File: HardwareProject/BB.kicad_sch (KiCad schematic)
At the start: 61 parts, among them J10 Conn_01x01, J11 Conn_01x01, J12 Conn_01x01, J9 Conn_01x01, Q1 HYG080N10LS1C2, Q2 HYG080N10LS1C2, Q3 HYG080N10LS1C2, Q4 HYG080N10LS1C2, U1 UCC27211ADRMR, U18 UCC27519, U2 UCC27211ADRMR, U3 UCC27519

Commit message: 修改了UCC27211A封装，此芯片此前的封装均错误 修改了采样线布局，为SAR ADC加入前置RC
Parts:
- U1, U2: footprint HPM6P41_BB:VSON-8-1EP_3x3mm_P0.65mm_EP1.65x2.4mm -> TexasInstruments:DRM8_3P38X2P45_TEX
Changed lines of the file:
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@@
 			)
 		)
-		(property "Footprint" "HPM6P41_BB:VSON-8-1EP_3x3mm_P0.65mm_EP1.65x2.4mm"
+		(property "Footprint" "TexasInstruments:DRM8_3P38X2P45_TEX"
 			(at 46.99 119.38 0)
 			(effects
@@
 			)
 		)
-		(property "Footprint" "HPM6P41_BB:VSON-8-1EP_3x3mm_P0.65mm_EP1.65x2.4mm"
+		(property "Footprint" "TexasInstruments:DRM8_3P38X2P45_TEX"
 			(at 138.43 119.38 0)
 			(effects

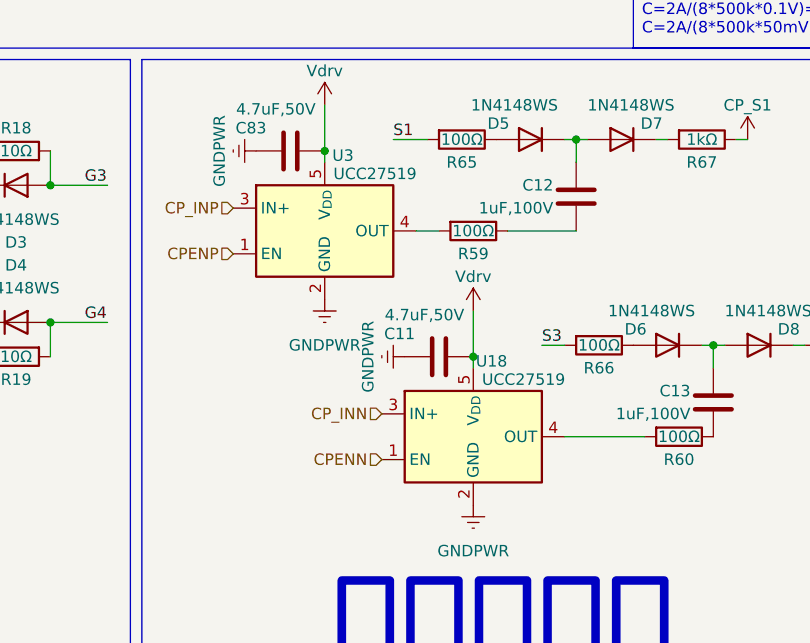
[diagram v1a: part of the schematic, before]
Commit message: 换掉UCC27519，它居然要55%VDD才到逻辑高，换成UCC2751
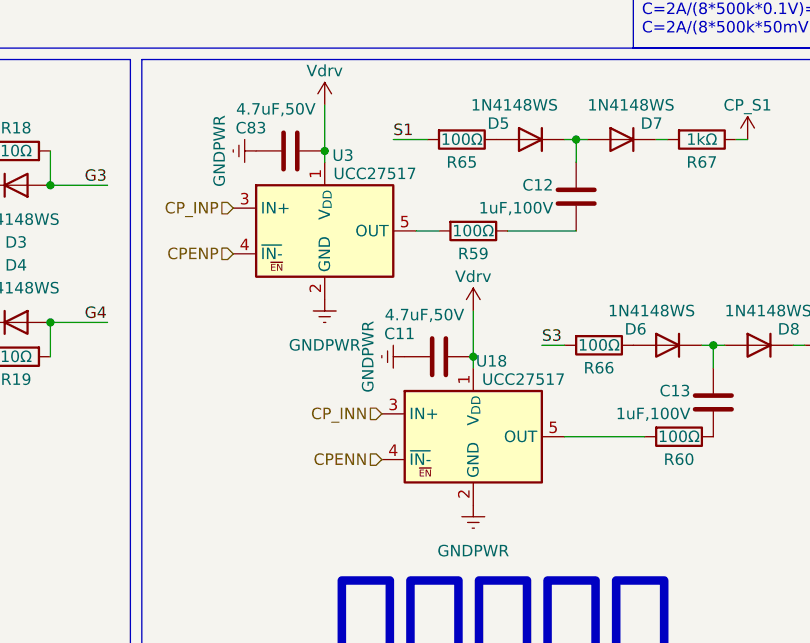
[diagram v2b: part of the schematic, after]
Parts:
- U18, U3: value UCC27519 -> UCC27517
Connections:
- net CPENN: now also U18.4 (~{IN-}); no longer U18.1 (EN)
- net CPENP: now also U3.4 (~{IN-}); no longer U3.1 (EN)
- net Vdrv: now also U18.1 (V_{DD}), U3.1 (V_{DD}); no longer U18.5 (V_{DD}), U3.5 (V_{DD})
- net at R60.2: now also U18.5 (OUT); no longer U18.4 (OUT)
- net at R59.2: now also U3.5 (OUT); no longer U3.4 (OUT)
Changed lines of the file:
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@@
+	)
+	(symbol
+		(lib_name "UCC27518_UCC27519_1")
+		(lib_id "1MyICs:UCC27518_UCC27519")
+		(at 236.22 140.97 0)
+		(unit 1)
+		(exclude_from_sim no)
+		(in_bom yes)
+		(on_board yes)
+		(dnp no)
+		(property "Reference" "U18"
+			(at 238.252 132.588 0)
+			(effects
+				(font
+					(size 1.27 1.27)
+				)
+			)
+		)
+		(property "Value" "UCC27517"
+			(at 241.808 134.62 0)
+			(effects
+				(font
+					(size 1.27 1.27)
+				)
+			)
+		)
+		(property "Footprint" "Package_TO_SOT_SMD:SOT-23-5"
+			(at 236.22 153.035 0)
+			(effects
+				(font
+					(size 1.27 1.27)
+				)
+				(hide yes)
+			)
+		)
+		(property "Datasheet" "https://www.ti.com.cn/cn/lit/ds/symlink/ucc27519.pdf?ts=1747047529320&ref_url=https%253A%252F%252Fwww.ti.com.cn%252Fproduct%252Fcn%252FUCC27519"
+			(at 236.22 121.92 0)
+			(effects
+				(font
+					(size 1.27 1.27)
+				)
+				(hide yes)
+			)
+		)
+		(property "Description" "Single-Channel High-Speed Low-Side Gate Driver With 4-A Peak Source and 8-A Peak Sink, SOT-23-6"
+			(at 236.22 140.97 0)
+			(effects
+				(font
+					(size 1.27 1.27)
+				)
+				(hide yes)
+			)
+		)
+		(pin "3"
+		)
+		(pin "1"
+		)
+		(pin "4"
+		)
+		(pin "5"
+		)
+		(pin "2"
+		)
+		(instances
+			(project "HPM6P41_BB"
+				(path "/714b8a30-f9a7-49d4-a000-bc20c4884c7a/89c5bb8e-77b8-47ed-968d-36636acd2e72"
+					(reference "U18")
+					(unit 1)
+				)
+			)
+		)
 	)
 	(symbol
@@
 	)
 	(symbol
-		(lib_id "1MyICs:UCC27518_UCC27519")
-		(at 236.22 140.97 0)
-		(unit 1)
-		(exclude_from_sim no)
-		(in_bom yes)
-		(on_board yes)
-		(dnp no)
-		(property "Reference" "U18"
-			(at 238.252 132.588 0)
-			(effects
-				(font
-					(size 1.27 1.27)
-				)
-			)
-		)
-		(property "Value" "UCC27519"
-			(at 241.808 134.62 0)
-			(effects
-				(font
-					(size 1.27 1.27)
-				)
-			)
-		)
-		(property "Footprint" "Package_TO_SOT_SMD:SOT-23-5"
-			(at 236.22 153.035 0)
-			(effects
-				(font
-					(size 1.27 1.27)
-				)
-				(hide yes)
-			)
-		)
-		(property "Datasheet" "https://www.ti.com.cn/cn/lit/ds/symlink/ucc27519.pdf?ts=1747047529320&ref_url=https%253A%252F%252Fwww.ti.com.cn%252Fproduct%252Fcn%252FUCC27519"
-			(at 236.22 121.92 0)
-			(effects
-				(font
-					(size 1.27 1.27)
-				)
-				(hide yes)
-			)
-		)
-		(property "Description" "Single-Channel High-Speed Low-Side Gate Driver With 4-A Peak Source and 8-A Peak Sink, SOT-23-6"
-			(at 236.22 140.97 0)
-			(effects
-				(font
-					(size 1.27 1.27)
-				)
-				(hide yes)
-			)
-		)
-		(pin "3"
-		)
-		(pin "1"
-		)
-		(pin "4"
-		)
-		(pin "5"
-		)
-		(pin "2"
-		)
-		(instances
-			(project "HPM6P41_BB"
-				(path "/714b8a30-f9a7-49d4-a000-bc20c4884c7a/89c5bb8e-77b8-47ed-968d-36636acd2e72"
-					(reference "U18")
-					(unit 1)
-				)
-			)
-		)
-	)
-	(symbol
 		(lib_id "power:+12V")
 		(at 27.94 113.03 0)
@@
 	)
 	(symbol
+		(lib_name "UCC27518_UCC27519_1")
 		(lib_id "1MyICs:UCC27518_UCC27519")
 		(at 219.71 118.11 0)
@@
 			)
 		)
-		(property "Value" "UCC27519"
+		(property "Value" "UCC27517"
 			(at 225.298 111.76 0)
 			(effects
@@
 		(instances
 			(project ""
-				(path "/714b8a30-f9a7-49d4-a000-bc20c4884c7a/89c5bb8e-77b8-47ed-968d-36636acd2e72"
+				(path "/714b8a30-f9a7-49d4-a000-bc20c4884c7a/5ba70b1a-2680-42f0-98ce-27de27e994eb"
 					(reference "U3")
+					(unit 1)
+				)
+				(path "/714b8a30-f9a7-49d4-a000-bc20c4884c7a/89c5bb8e-77b8-47ed-968d-36636acd2e72"
+					(reference "U3")

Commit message: Rev3最终版本
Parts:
- added TP1, TP2, TP3, TP4: TestPoint_Probe, HPM6P41_BB:TestPoint_Bridge_Pitch1.2mm_Drill0.7mm, symbol Connector:TestPoint_Probe
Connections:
- net IN1: now also TP3.1
- net IN2: now also TP4.1
- net IN3: now also TP1.1
- net IN4: now also TP2.1

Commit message: 换其他电感之前暂存一下
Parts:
- removed R17: 1mΩ 5W, HPM6P41_BB:R_Shunt_2725_2726, symbol Device:R_Shunt
- added C80, C84, C85, C94: 100V 100uF, Capacitor_THT:CP_Radial_D10.0mm_P5.00mm, symbol Device:C_Polarized
- C10, C3, C4, C9: footprint HPM6P41_BB:CP_Radial_D10.0mm_P5.00mm -> Capacitor_THT:CP_Radial_D10.0mm_P5.00mm
- L1: value CPU2916-6R8MC/VER2923-682KL -> PQ26XX; footprint HPM6P41_BB:IND_VER2923_COC -> HPM6P41_BB:PQ26XX
- TP1, TP2, TP3, TP4: footprint HPM6P41_BB:TestPoint_Bridge_Pitch1.2mm_Drill0.7mm -> HPM6P41_BB:测试点
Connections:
- net GNDPWR: now also C80.2, C84.2, C85.2, C94.2
- net S1: now also L1.2; no longer L1.1
- net S3: now also R10.1; no longer L1.2
- net VIN: now also Q1.5 (D), C85.1, C94.1; no longer R10.1
- net VOUT: now also Q3.5 (D), C80.1, C84.1
- net at R10.4: now also L1.1; no longer Q1.5 (D)
- net InputIsense+ renamed ISENSE-
- net InputIsense- renamed ISENSE+
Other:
- moved on the sheet: C8, C9, J11, J12, L1, Q3, Q4, R10, R15, R16, R20, R21

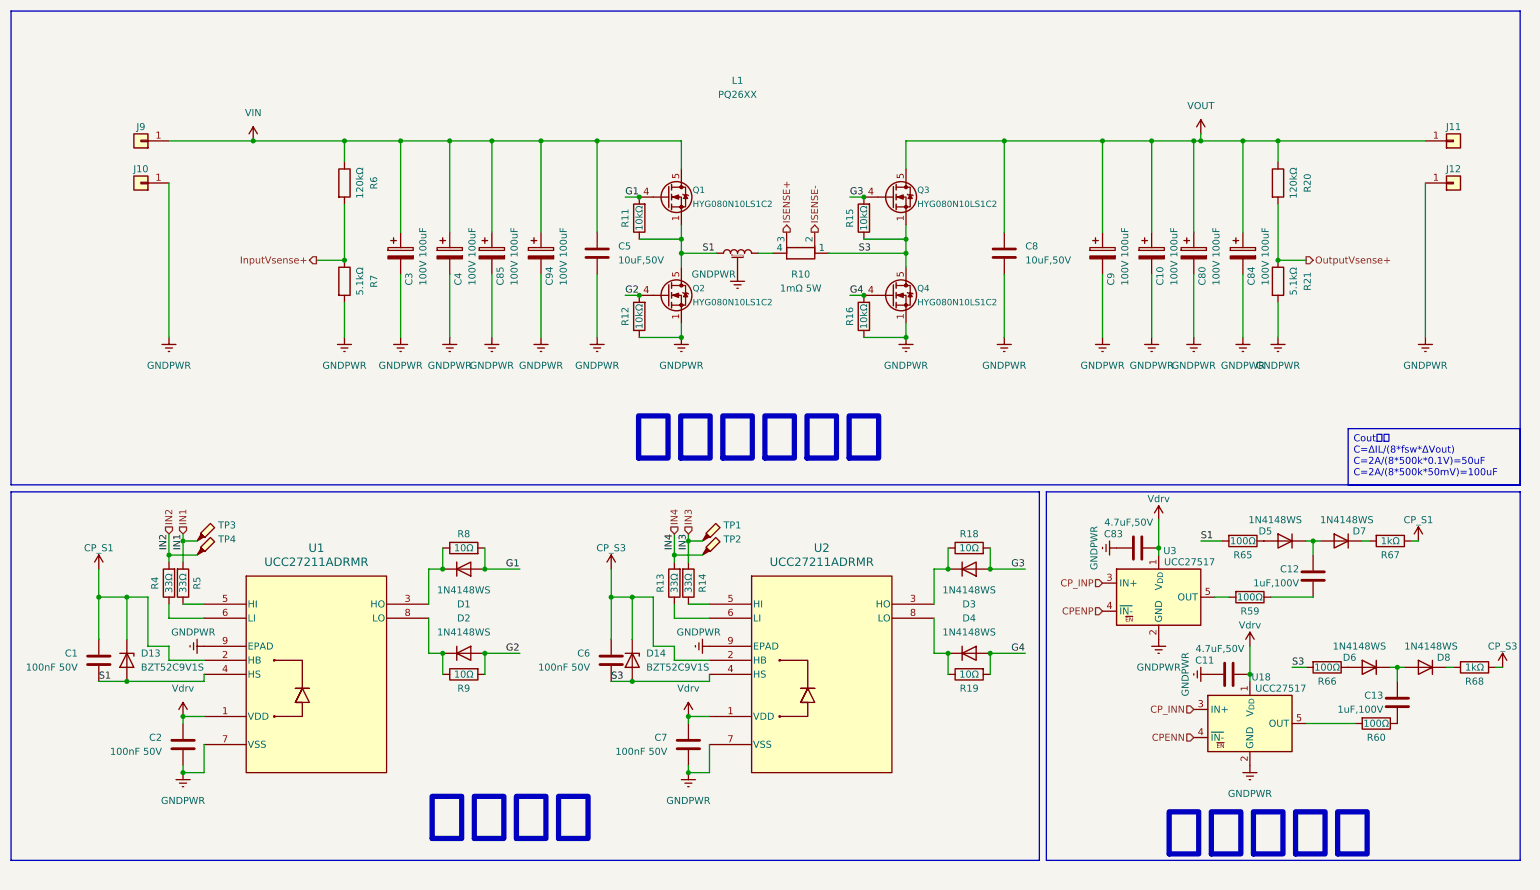
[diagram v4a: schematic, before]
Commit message: 完成Rev4 电源 驱动 模拟 IO
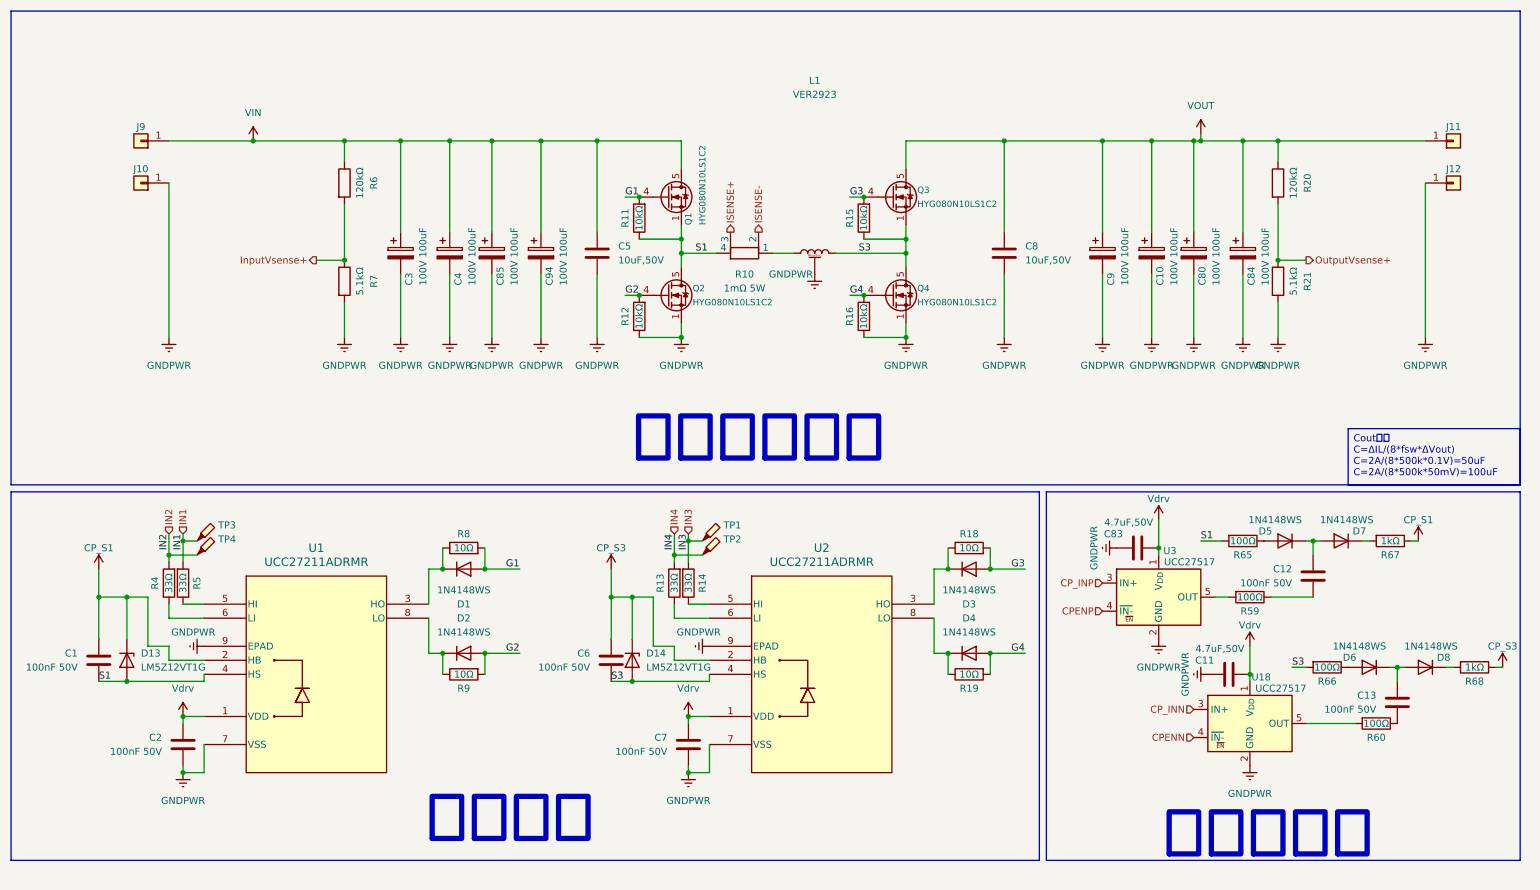
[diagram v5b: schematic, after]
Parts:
- C12, C13: value 1uF,100V -> 100nF 50V; footprint Capacitor_SMD:C_0805_2012Metric -> Capacitor_SMD:C_0603_1608Metric
- D1, D2, D3, D4, D5, D6, D7, D8: footprint Diode_SMD:D_SOD-323 -> Diode_SMD:D_SOD-523
- D13, D14: value BZT52C9V1S -> LM5Z12VT1G; footprint Diode_SMD:D_SOD-323 -> Diode_SMD:D_SOD-523
- L1: value PQ26XX -> VER2923; footprint HPM6P41_BB:PQ26XX -> HPM6P41_BB:IND_VER2923_COC
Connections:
- net S1: now also R10.4; no longer L1.2
- net S3: now also L1.2; no longer R10.1
- net at L1.1: now also R10.1; no longer R10.4
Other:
- moved on the sheet: L1, R10

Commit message: rev4修改核心供电前保存（当前SYR838）
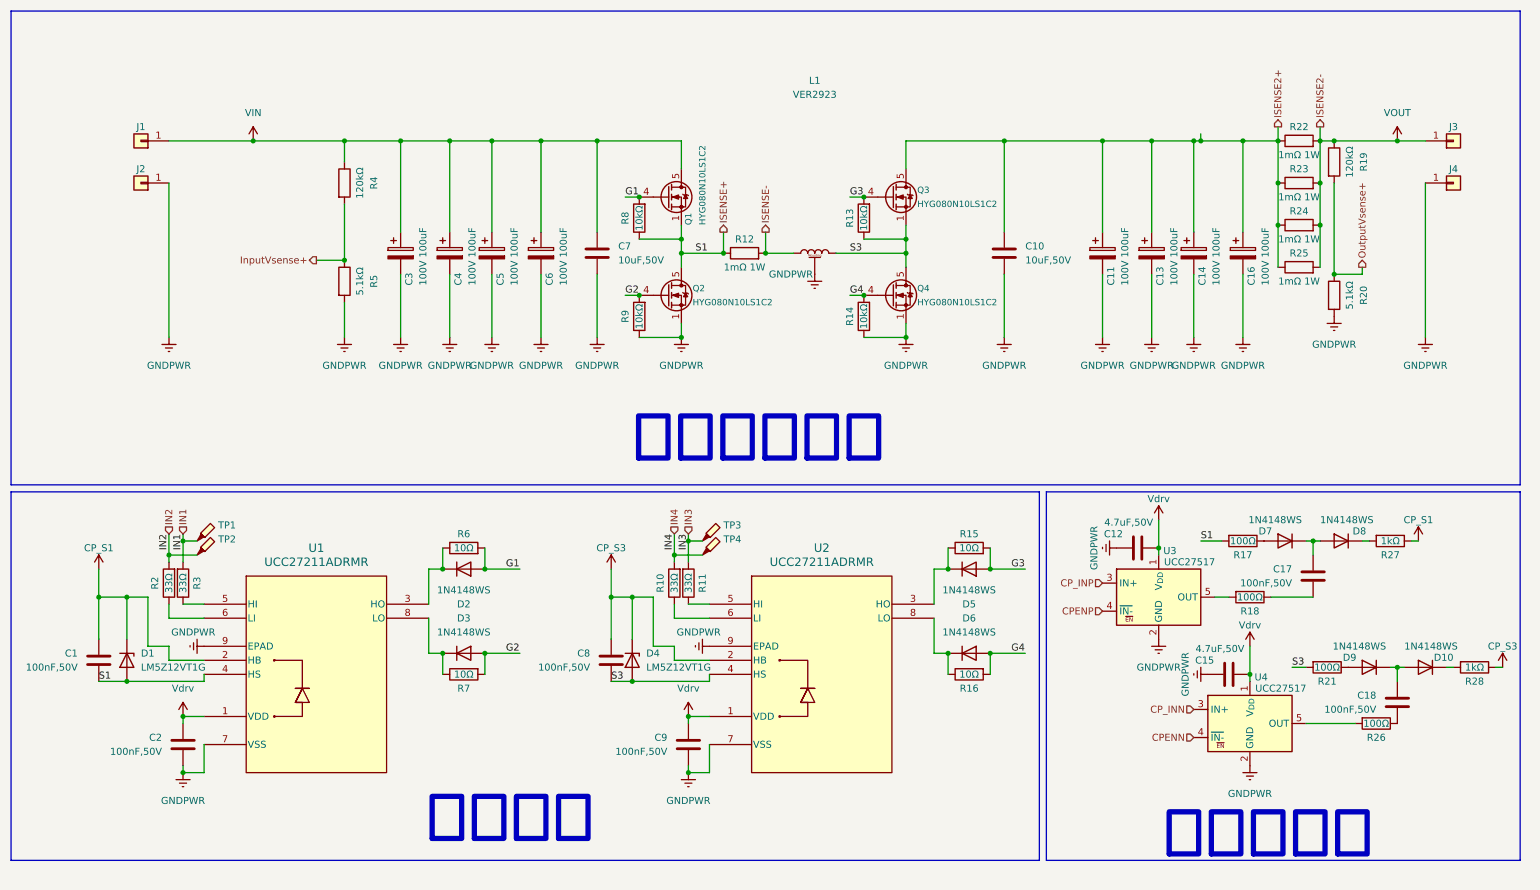
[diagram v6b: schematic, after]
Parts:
- removed R10: 1mΩ 5W, HPM6P41_BB:R_Shunt_2725_2726, symbol Device:R_Shunt
- added R12, R22, R23, R24, R25: 1mΩ 1W, Resistor_SMD:R_0612_1632Metric, symbol Device:R
- C1, C2: value 100nF 50V -> 100nF,50V
- C17: renamed from C12; value 100nF 50V -> 100nF,50V
- C18: renamed from C13; value 100nF 50V -> 100nF,50V
- C8: renamed from C6; value 100nF 50V -> 100nF,50V
- C9: renamed from C7; value 100nF 50V -> 100nF,50V
- renumbered C8 to C10, C9 to C11, C83 to C12, C10 to C13, C80 to C14, C11 to C15, C84 to C16, C85 to C5, C94 to C6, C5 to C7, D13 to D1, D8 to D10, D1 to D2, D2 to D3, D14 to D4, D3 to D5, D4 to D6, D5 to D7, D7 to D8, D6 to D9, J9 to J1, J10 to J2, J11 to J3, J12 to J4, R13 to R10, R14 to R11, R15 to R13, R16 to R14, R18 to R15, R19 to R16, R65 to R17, R59 to R18, R20 to R19, R4 to R2, R21 to R20, R66 to R21, R60 to R26, R67 to R27, R68 to R28, R5 to R3, R6 to R4, R7 to R5, R8 to R6, R9 to R7, R11 to R8, R12 to R9, TP3 to TP1, TP4 to TP2, TP1 to TP3, TP2 to TP4, U18 to U4
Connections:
- net S1 is gone; now on net ISENSE+: C1.2, D1.2 (A), Q1.1 (S), Q1.2 (S), Q1.3 (S), Q2.5 (D), R17.2, R8.1, U1.4 (HS)
- net ISENSE+: now also R12.1
- net ISENSE-: now also L1.1, R12.2
- net VOUT: now also R22.2, R23.2, R24.2, R25.2; no longer C10.1, C11.1, C13.1, C14.1, C16.1, Q3.5 (D)
- new net ISENSE2+: C10.1, C11.1, C13.1, C14.1, C16.1, Q3.5 (D), R22.1, R23.1, R24.1, R25.1
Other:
- moved on the sheet: R19, R20
